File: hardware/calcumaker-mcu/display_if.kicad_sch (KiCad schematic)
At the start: 12 parts, among them J3 TO DISPLAY (FFC), U5 TPS61022RWUR, U6 74HCT125

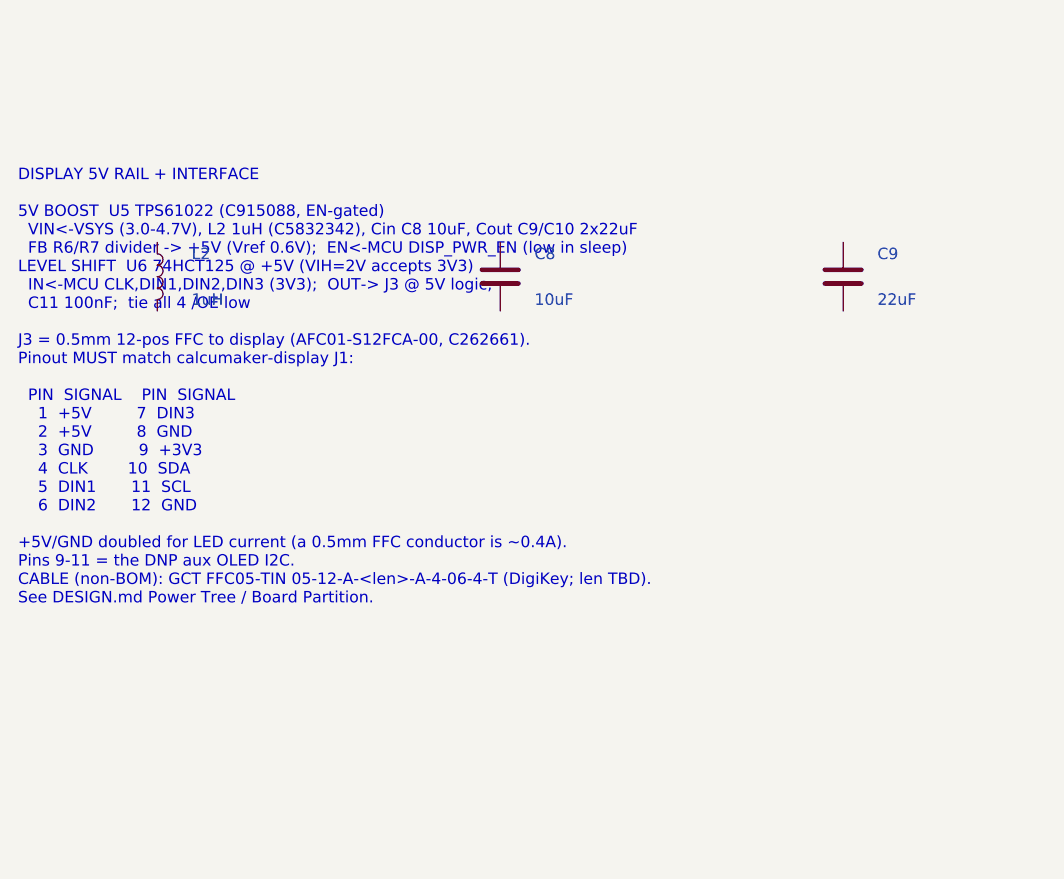
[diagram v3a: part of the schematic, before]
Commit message: hardware: per-key RGB hint lighting on the keyboard board (50x SK6805 on gated VSYS) (#4)
Add addressable RGB accent lighting that hints key positions / presses -- one
SK6805-EC15 (1.5x1.5mm, the smallest serial RGB with a KiCad footprint + real
LCSC stock, C2890035) beside each of the 50 keys, single-wire daisy chain off
one STM32G0 pin.

Power: the LEDs are ~5V parts and the keyboard rail is only 3.3V, so they run
off VSYS (the MCU board's load-shared battery/USB rail, ~3.7-4.7V) brought up a
WIDENED 12-pin mezzanine (10 -> 12: +VSYS +GND). A high-side P-FET load switch
(Q1 AO3401A + Q2 2N7002) gates the whole LED rail off in sleep (G0 LED_EN) to
protect battery life, and a 74LVC1G125 (powered from the gated rail) level-shifts
the 3.3V data up to the LED VIH.

- calcumaker-keyboard: new KeyLighting sheet (50x SK6805 D56-D105 + U2 shifter +
  Q1/Q2 load switch + R7-R10 / C6-C7); J1 mezzanine -> 12-pin DF40C-12DP
  (C6224952). 119 -> 178 components.
- calcumaker-mcu: J5 mezzanine -> 12-pin DF40B-12DS (C3641147); route VSYS.
- DF40 stack: the receptacle SUFFIX sets the mated height (none = 1.5mm,
  (2.0) = 2.0mm, H-series = 2.5-4.0mm), NOT the B/C letter; the DF40C plug is the
  common header -- so DF40C-12DP x DF40B-12DS is a valid 1.5mm stack, same as the
  original 10-pin (DF40C-12DS just isn't LCSC-stocked).
- DESIGN.md / PARTS.md / memory: RGB subsystem, 12-pin pinout, BOM rows, the
  sleep-gate + current-cap notes (firmware must cap total brightness; 50x
  full-white ~0.75A would exceed the DF40 / VSYS budget).

All three boards regenerate + pass the structure check (mcu 55 / keyboard 178 /
display 60, no duplicate refs).

Co-authored-by: Claude Opus 4.8 (1M context) <noreply@anthropic.com>
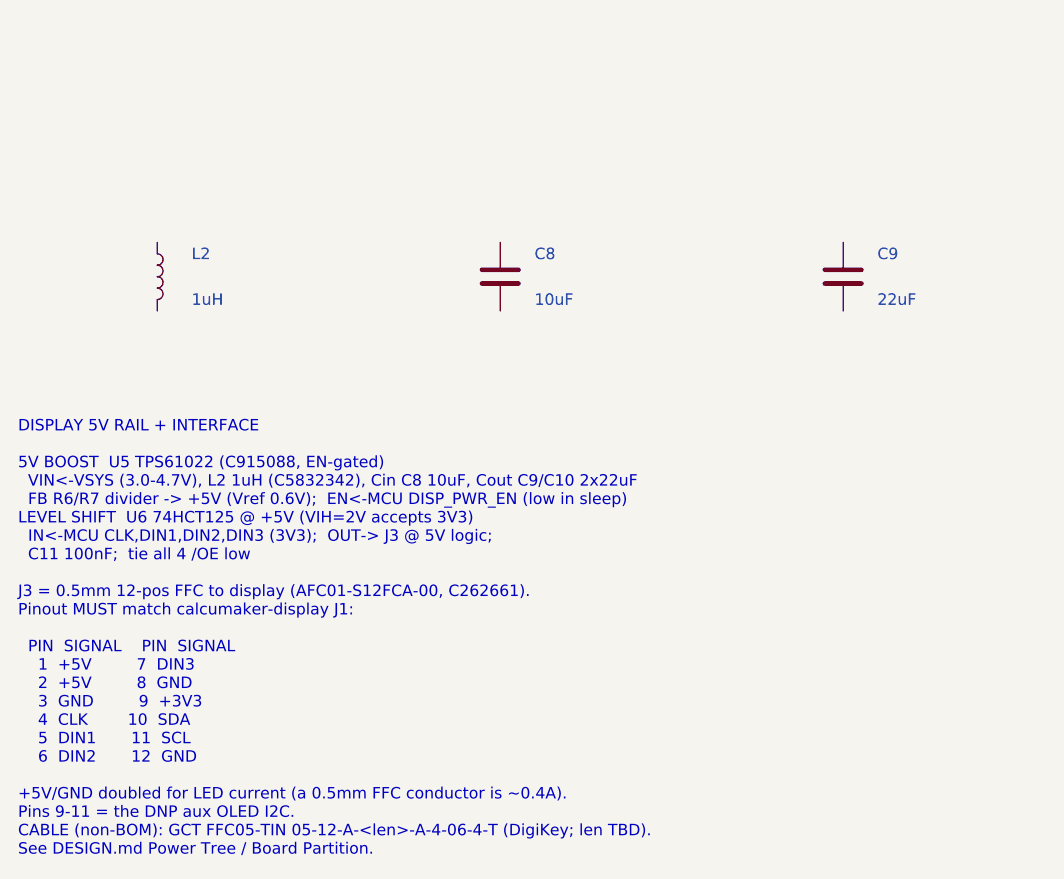
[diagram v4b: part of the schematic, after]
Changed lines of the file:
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@@
 	(text "DISPLAY 5V RAIL + INTERFACE\n\n5V BOOST  U5 TPS61022 (C915088, EN-gated)\n  VIN<-VSYS (3.0-4.7V), L2 1uH (C5832342), Cin C8 10uF, Cout C9/C10 2x22uF\n  FB R6/R7 divider -> +5V (Vref 0.6V);  EN<-MCU DISP_PWR_EN (low in sleep)\nLEVEL SHIFT  U6 74HCT125 @ +5V (VIH=2V accepts 3V3)\n  IN<-MCU CLK,DIN1,DIN2,DIN3 (3V3);  OUT-> J3 @ 5V logic;\n  C11 100nF;  tie all 4 /OE low\n\nJ3 = 0.5mm 12-pos FFC to display (AFC01-S12FCA-00, C262661).\nPinout MUST match calcumaker-display J1:\n\n  PIN  SIGNAL    PIN  SIGNAL\n    1  +5V         7  DIN3  \n    2  +5V         8  GND   \n    3  GND         9  +3V3  \n    4  CLK        10  SDA   \n    5  DIN1       11  SCL   \n    6  DIN2       12  GND\n\n+5V/GND doubled for LED current (a 0.5mm FFC conductor is ~0.4A).\nPins 9-11 = the DNP aux OLED I2C.\nCABLE (non-BOM): GCT FFC05-TIN 05-12-A-<len>-A-4-06-4-T (DigiKey; len TBD).\nSee DESIGN.md Power Tree / Board Partition."
 		(exclude_from_sim no)
-		(at 15.00 110.00 0)
+		(at 15.00 137.92 0)
 		(effects (font (face "Courier New") (size 1.27 1.27)) (justify left top))
 	)

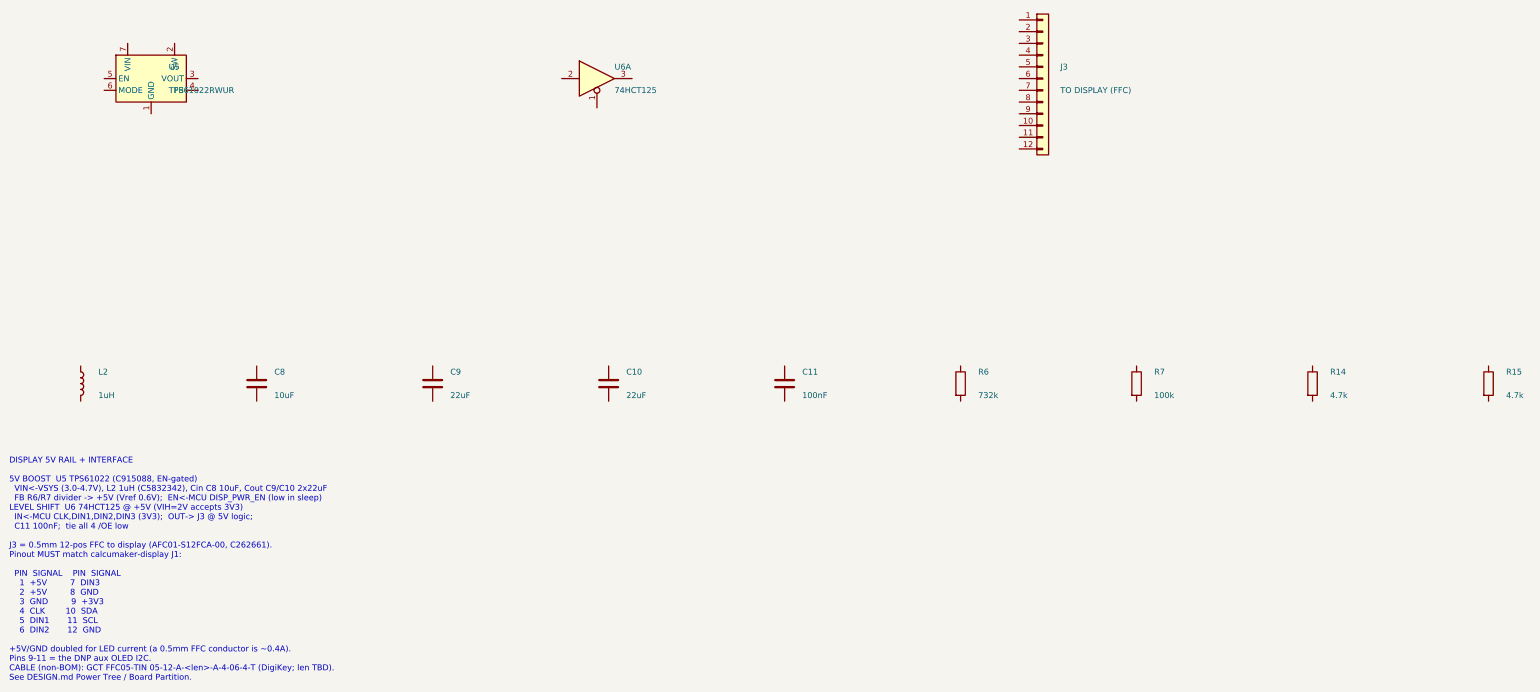
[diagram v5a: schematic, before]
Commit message: hardware: unified SPI display-module interface + RGB dot-matrix board
Make the display a swappable module on ONE technology-agnostic connector
(mirrors the keyboard-G0 pattern): the MCU board speaks a single SPI
"display intent" bus and each display board carries its own MCU that
renders locally. Two interchangeable modules on the same 12-pin FFC.

- calcumaker-matrix (NEW): full-color RGB dot matrix, 96x24 = 2304x 1mm
  XL-1010RGBC-2812B-S (C51900942) driven by an RP2040 (PIO). Nested
  multi-channel: led_cluster (8x8) x12 -> led_row (768px chain) x3.
  Dedicated VSYS LED-power inlet keeps amps off the signal FFC. Authored
  the 1mm 1010 footprint; RP2040/flash/shifter symbols are stock.
- calcumaker-display (7-seg): retrofit to a smart module -- added an
  STM32G031 SPI slave, and moved the 5V boost (TPS61022) + 74HCT125
  shifter off the MCU board onto it. Interconnect reworked CLK/DIN -> SPI.
- calcumaker-mcu: DisplayIF simplified to the unified SPI connector +
  a 2-pin VSYS outlet for the matrix LED rail.

Unified pinout (mcu J3 / display J1 / matrix J1): VSYS,VSYS,GND,GND,+3V3,
SPI_SCLK,SPI_MOSI,SPI_CS,DISP_IRQ,DISP_NRST,DISP_BOOT,GND.

All boards generate + check clean (mcu 46 / keyboard 179 / display 77 /
matrix 2339, no dup refs). Docs (PARTS.md, DESIGN.md, Makefile) updated.
Firmware is deferred; the SPI contract is documented so it is unblocked.

Co-Authored-By: Claude Opus 4.8 (1M context) <noreply@anthropic.com>
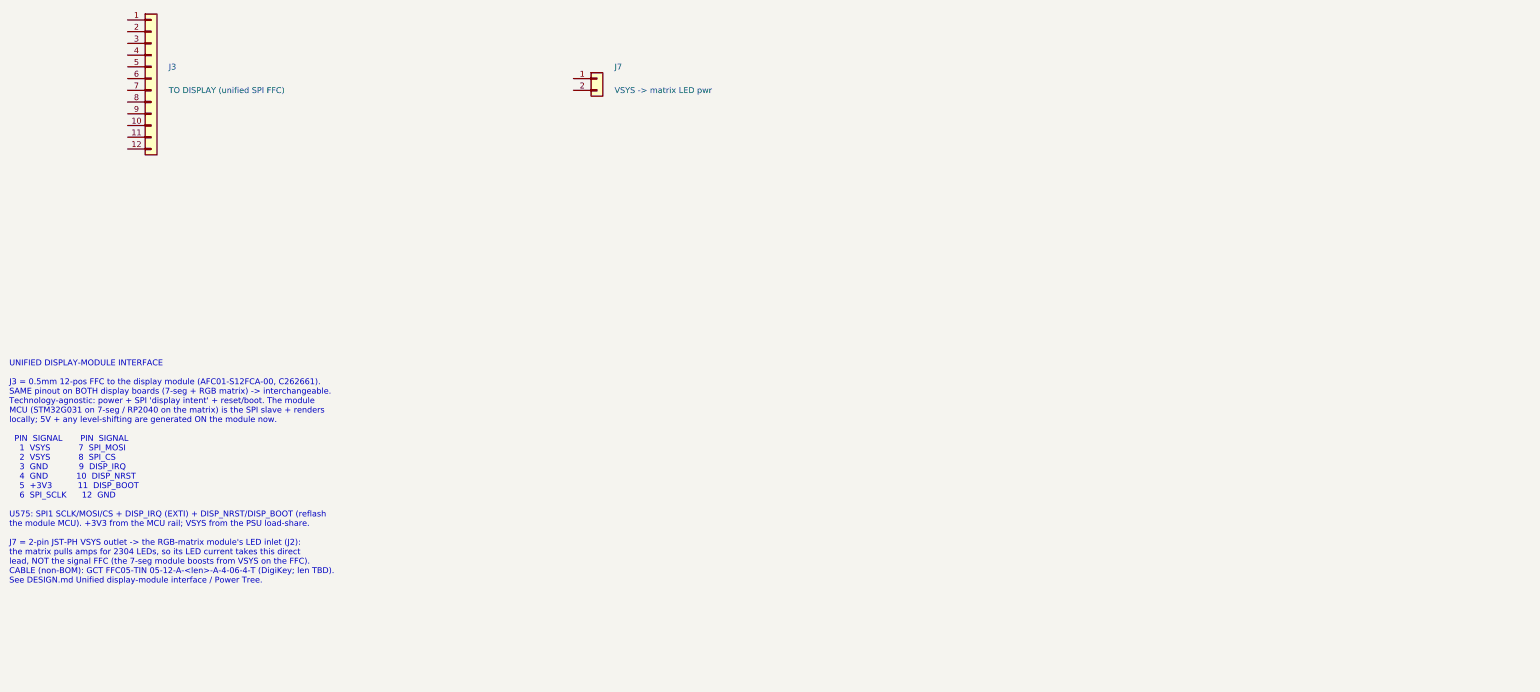
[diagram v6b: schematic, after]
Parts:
- removed C10, C9: 22uF, Capacitor_SMD:C_0603_1608Metric, symbol Device:C
- removed C11: 100nF, Capacitor_SMD:C_0402_1005Metric, symbol Device:C
- removed C8: 10uF, Capacitor_SMD:C_0603_1608Metric, symbol Device:C
- removed L2: 1uH, Inductor_SMD:L_0805_2012Metric, symbol Device:L
- removed R14, R15: 4.7k, Resistor_SMD:R_0402_1005Metric, symbol Device:R
- removed R6: 732k, Resistor_SMD:R_0402_1005Metric, symbol Device:R
- removed R7: 100k, Resistor_SMD:R_0402_1005Metric, symbol Device:R
- removed U5: TPS61022RWUR, Package_DFN_QFN:Texas_RWU0007A_VQFN-7_2x2mm_P0.5mm, symbol Converter_DCDC:TPS61022
- removed U6: 74HCT125, Package_SO:SOIC-14_3.9x8.7mm_P1.27mm, symbol 74xx:74AHCT125
- added J7: VSYS -> matrix LED pwr, Connector_JST:JST_PH_S2B-PH-K_1x02_P2.00mm_Horizontal, symbol Connector_Generic:Conn_01x02
- J3: value TO DISPLAY (FFC) -> TO DISPLAY (unified SPI FFC)
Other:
- note added: "UNIFIED DISPLAY-MODULE INTERFACE J3 = 0.5mm 12-pos FFC to the display module (AFC01-S12FCA-00, C262661). SAME pinout on BOTH display boards (7-seg + RGB matrix) -> interchangeable. Technology-agnostic: power + SPI 'display intent' + reset/boot. The module MCU (STM32G031 on 7-seg / RP2040 on the matrix) is the SPI slave + renders locally; 5V + any level-shifting are generated ON the module now. PI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"
- note removed: "DISPLAY 5V RAIL + INTERFACE 5V BOOST U5 TPS61022 (C915088, EN-gated) VIN<-VSYS (3.0-4.7V), L2 1uH (C5832342), Cin C8 10uF, Cout C9/C10 2x22uF FB R6/R7 divider -> +5V (Vref 0.6V); EN<-MCU DISP_PWR_EN (low in sleep) LEVEL SHIFT U6 74HCT125 @ +5V (VIH=2V accepts 3V3) IN<-MCU CLK,DIN1,DIN2,DIN3 (3V3); OUT-> J3 @ 5V logic; C11 100nF; tie all 4 /OE low J3 = 0.5mm 12-pos FFC to display (AFC01-S12FCA-00,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"
- title: Calcumaker 16 — MCU — Display 5V rail (TPS61022) + 74HCT125 level shifter + interconnect -> Calcumaker 16 — MCU — Unified display-module interface (SPI FFC J3 + VSYS outlet J7)
